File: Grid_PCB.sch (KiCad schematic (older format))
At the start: 8 parts, among them J10 LED_Conn, J9 ESP_Conn, U1 SN74HC151N

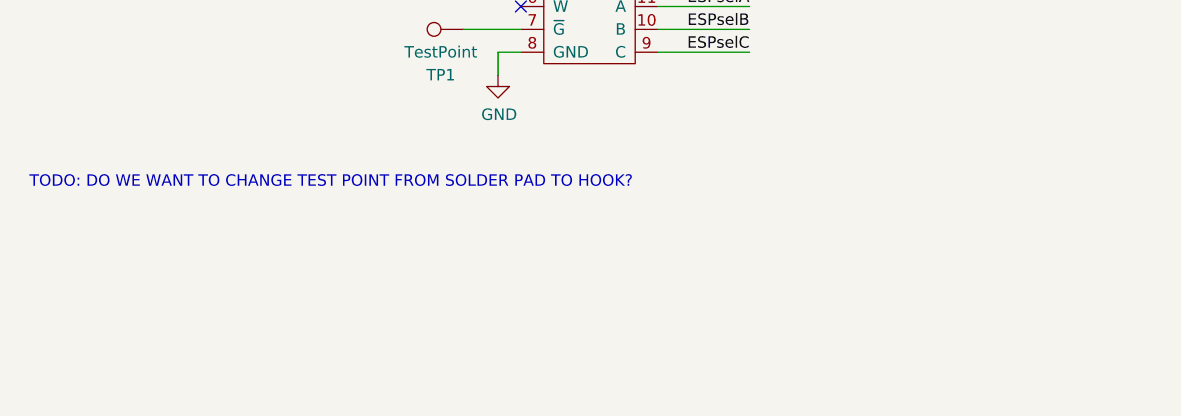
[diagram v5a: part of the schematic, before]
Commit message: updated with todo for routing around screws
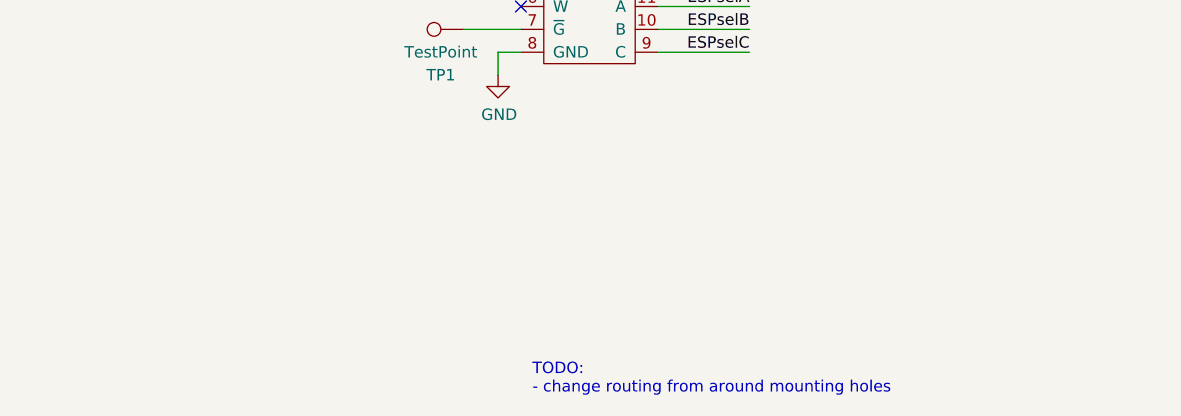
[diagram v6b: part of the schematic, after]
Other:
- note added: "TODO: \n- change routing from around mounting holes"
- note removed: "TODO: DO WE WANT TO CHANGE TEST POINT FROM SOLDER PAD TO HOOK?"
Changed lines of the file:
@@
 Wire Wire Line
 	6850 4800 7550 4800
-Text Notes 800  5600 0    50   ~ 0
-TODO: DO WE WANT TO CHANGE TEST POINT FROM SOLDER PAD TO HOOK?
+Text Notes 3000 6500 0    50   ~ 0
+TODO: \n- change routing from around mounting holes
 NoConn ~ 2950 4800
 Text Label 2550 4700 0    50   ~ 0

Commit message: flipped components to back side
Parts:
- removed TP1: TestPoint, TestPoint:TestPoint_Pad_2.5x2.5mm, symbol Connector:TestPoint
- added J11: ESP_Conn, Connector_JST:JST_EH_B2B-EH-A_1x02_P2.50mm_Vertical, symbol grid:ESP_Conn
- J10: footprint Connector_PinHeader_2.54mm:PinHeader_1x02_P2.54mm_Horizontal -> Connector_JST:JST_EH_B2B-EH-A_1x02_P2.50mm_Vertical
- J9: footprint Connector_PinHeader_2.54mm:PinHeader_1x07_P2.54mm_Horizontal -> Connector_JST:JST_EH_B5B-EH-A_1x05_P2.50mm_Vertical; symbol grid:ESP_Conn -> Connector:Conn_01x05_Female
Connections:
- wire segments 44 -> 43
- no-connect marks 1 -> 2
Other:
- note added: "ESP Connector"
- note added: "Input Multiplexer"
- note added: "Input/LED Nodes"
- note added: "LED Daisy Chain Connector"
- note added: "Mounting Holes"
- note removed: "Note the order of these can be changed for ease of routing\njust needs to match up with esp connector (or not, we could just change\norientations/ordering in the cables)"
- note removed: "PCB for one row of BOTH the attack or position grid"
- note removed: "TODO: \n- change routing from around mounting holes"
- note removed: "Using 7/16" standoff \n(11.13mm tall, 6.35mm diam)\n** Can be changed later **"
- moved on the sheet: H1, H2, H3, H4, J10, U1

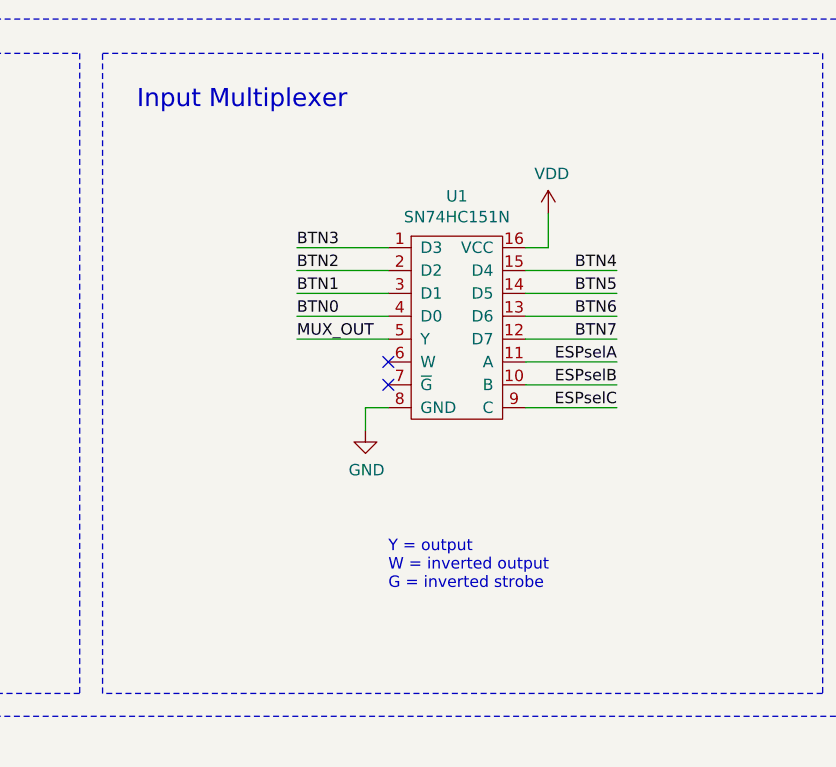
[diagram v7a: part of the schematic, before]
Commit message: fixed added cap for mux and fixed drc errors
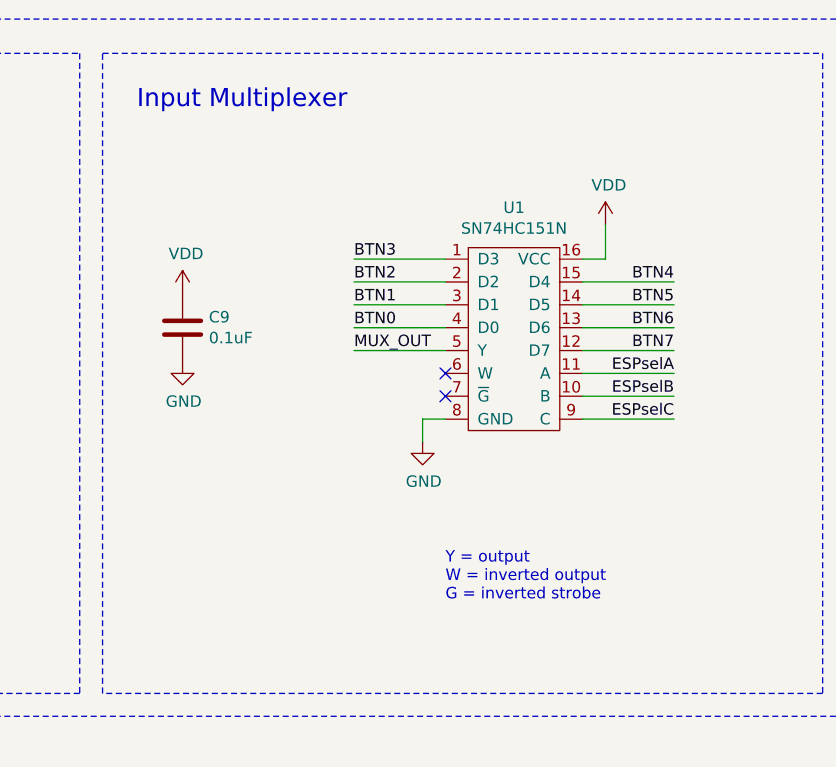
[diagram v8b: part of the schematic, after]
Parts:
- added C9: 0.1uF, Capacitor_SMD:C_0805_2012Metric_Pad1.18x1.45mm_HandSolder, symbol Device:C
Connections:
- net GND: now also C9.2
- net VDD: now also C9.1
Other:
- moved on the sheet: U1
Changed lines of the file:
@@
 L power:VDD #PWR01
 U 1 1 61484263
-P 5650 4350
-F 0 "#PWR01" H 5650 4200 50  0001 C CNN
-F 1 "VDD" H 5665 4523 50  0000 C CNN
-F 2 "" H 5650 4350 50  0001 C CNN
-F 3 "" H 5650 4350 50  0001 C CNN
-	1    5650 4350
-	1    0    0    -1
-$EndComp
-Text Label 4550 4800 0    50   ~ 0
+P 5900 4400
+F 0 "#PWR01" H 5900 4250 50  0001 C CNN
+F 1 "VDD" H 5915 4573 50  0000 C CNN
+F 2 "" H 5900 4400 50  0001 C CNN
+F 3 "" H 5900 4400 50  0001 C CNN
+	1    5900 4400
+	1    0    0    -1
+$EndComp
+Text Label 4800 4850 0    50   ~ 0
 BTN0
 Wire Wire Line
-	4550 4800 4950 4800
+	4800 4850 5200 4850
 $Sheet
 S 3350 1400 800  350
@@
 L grid:SN74HC151N U1
 U 1 1 61544325
-P 5250 4850
-F 0 "U1" H 5250 5425 50  0000 C CNN
-F 1 "SN74HC151N" H 5250 5334 50  0000 C CNN
-F 2 "Package_DIP:DIP-16_W10.16mm" H 5300 4850 50  0001 C CNN
-F 3 "https://www.ti.com/lit/ds/symlink/sn74hc151.pdf?ts=1632846774937&ref_url=https%253A%252F%252Fwww.google.com%252F" H 5300 4850 50  0001 C CNN
-	1    5250 4850
-	1    0    0    -1
-$EndComp
-Text Label 4550 4700 0    50   ~ 0
+P 5500 4900
+F 0 "U1" H 5500 5475 50  0000 C CNN
+F 1 "SN74HC151N" H 5500 5384 50  0000 C CNN
+F 2 "Package_DIP:DIP-16_W10.16mm" H 5550 4900 50  0001 C CNN
+F 3 "https://www.ti.com/lit/ds/symlink/sn74hc151.pdf?ts=1632846774937&ref_url=https%253A%252F%252Fwww.google.com%252F" H 5550 4900 50  0001 C CNN
+	1    5500 4900
+	1    0    0    -1
+$EndComp
+Text Label 4800 4750 0    50   ~ 0
 BTN1
 Wire Wire Line
-	4550 4700 4950 4700
-Text Label 4550 4600 0    50   ~ 0
+	4800 4750 5200 4750
+Text Label 4800 4650 0    50   ~ 0
 BTN2
 Wire Wire Line
-	4550 4600 4950 4600
-Text Label 4550 4500 0    50   ~ 0
+	4800 4650 5200 4650
+Text Label 4800 4550 0    50   ~ 0
 BTN3
 Wire Wire Line
-	4550 4500 4950 4500
-Text Label 5950 4600 2    50   ~ 0
+	4800 4550 5200 4550
+Text Label 6200 4650 2    50   ~ 0
 BTN4
 Wire Wire Line
-	5950 4600 5550 4600
-Text Label 5950 4700 2    50   ~ 0
+	6200 4650 5800 4650
+Text Label 6200 4750 2    50   ~ 0
 BTN5
 Wire Wire Line
-	5950 4700 5550 4700
-Text Label 5950 4800 2    50   ~ 0
+	6200 4750 5800 4750
+Text Label 6200 4850 2    50   ~ 0
 BTN6
 Wire Wire Line
-	5950 4800 5550 4800
-Text Label 5950 4900 2    50   ~ 0
+	6200 4850 5800 4850
+Text Label 6200 4950 2    50   ~ 0
 BTN7
 Wire Wire Line
-	5950 4900 5550 4900
+	6200 4950 5800 4950
 $Comp
 L power:GND #PWR02
 U 1 1 6148489C
-P 4850 5300
-F 0 "#PWR02" H 4850 5050 50  0001 C CNN
-F 1 "GND" H 4855 5127 50  0000 C CNN
-F 2 "" H 4850 5300 50  0001 C CNN
-F 3 "" H 4850 5300 50  0001 C CNN
-	1    4850 5300
-	1    0    0    -1
-$EndComp
-Wire Wire Line
-	5550 4500 5650 4500
-Wire Wire Line
-	5650 4500 5650 4350
-Wire Wire Line
-	4950 5200 4850 5200
-Wire Wire Line
-	4850 5200 4850 5300
-Text Label 5950 5000 2    50   ~ 0
+P 5100 5350
+F 0 "#PWR02" H 5100 5100 50  0001 C CNN
+F 1 "GND" H 5105 5177 50  0000 C CNN
+F 2 "" H 5100 5350 50  0001 C CNN
+F 3 "" H 5100 5350 50  0001 C CNN
+	1    5100 5350
+	1    0    0    -1
+$EndComp
+Wire Wire Line
+	5800 4550 5900 4550
+Wire Wire Line
+	5900 4550 5900 4400
+Wire Wire Line
+	5200 5250 5100 5250
+Wire Wire Line
+	5100 5250 5100 5350
+Text Label 6200 5050 2    50   ~ 0
 ESPselA
 Wire Wire Line
-	5950 5000 5550 5000
-Wire Wire Line
-	5950 5100 5550 5100
-Text Label 5950 5200 2    50   ~ 0
+	6200 5050 5800 5050
+Wire Wire Line
+	6200 5150 5800 5150
+Text Label 6200 5250 2    50   ~ 0
 ESPselC
 Wire Wire Line
-	5950 5200 5550 5200
-Text Label 5950 5100 2    50   ~ 0
+	6200 5250 5800 5250
+Text Label 6200 5150 2    50   ~ 0
 ESPselB
-Text Notes 4950 6000 0    50   ~ 0
+Text Notes 5200 6050 0    50   ~ 0
 Y = output\nW = inverted output\nG = inverted strobe
 $Sheet
@@
 Wire Wire Line
 	1750 4700 2450 4700
-NoConn ~ 4950 5000
-Text Label 4550 4900 0    50   ~ 0
+NoConn ~ 5200 5050
+Text Label 4800 4950 0    50   ~ 0
 MUX_OUT
 Wire Wire Line
-	4550 4900 4950 4900
+	4800 4950 5200 4950
 Text Label 2450 4700 2    50   ~ 0
 MUX_OUT
@@
 	1    0    0    -1
 $EndComp
-NoConn ~ 4950 5100
+NoConn ~ 5200 5150
+$Comp
+L Device:C C9
+U 1 1 61664AB9
+P 4050 4850
+F 0 "C9" H 4165 4896 50  0000 L CNN
+F 1 "0.1uF" H 4165 4805 50  0000 L CNN
+F 2 "Capacitor_SMD:C_0805_2012Metric_Pad1.18x1.45mm_HandSolder" H 4088 4700 50  0001 C CNN
+F 3 "~" H 4050 4850 50  0001 C CNN
+	1    4050 4850
+	1    0    0    -1
+$EndComp
+$Comp
+L power:GND #PWR014
+U 1 1 61664EA9
+P 4050 5000
+F 0 "#PWR014" H 4050 4750 50  0001 C CNN
+F 1 "GND" H 4055 4827 50  0000 C CNN
+F 2 "" H 4050 5000 50  0001 C CNN
+F 3 "" H 4050 5000 50  0001 C CNN
+	1    4050 5000
+	1    0    0    -1
+$EndComp
+$Comp
+L power:VDD #PWR06
+U 1 1 61665150
+P 4050 4700
+F 0 "#PWR06" H 4050 4550 50  0001 C CNN
+F 1 "VDD" H 4065 4873 50  0000 C CNN
+F 2 "" H 4050 4700 50  0001 C CNN
+F 3 "" H 4050 4700 50  0001 C CNN
+	1    4050 4700
+	1    0    0    -1
+$EndComp
 $EndSCHEMATC
